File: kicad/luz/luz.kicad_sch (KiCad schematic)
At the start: 58 parts, among them J1 Barrel_Jack, J2 Screw_Terminal_01x04, Q1 AO3400A, Q4 AO3400A, U1 U261-241N-4BS2SS, U2 CYPD3177-24LQXQ_C2959321, U3 SI4909DY-VB, U4 TPS54302, U5 ESP32-WROOM-32D

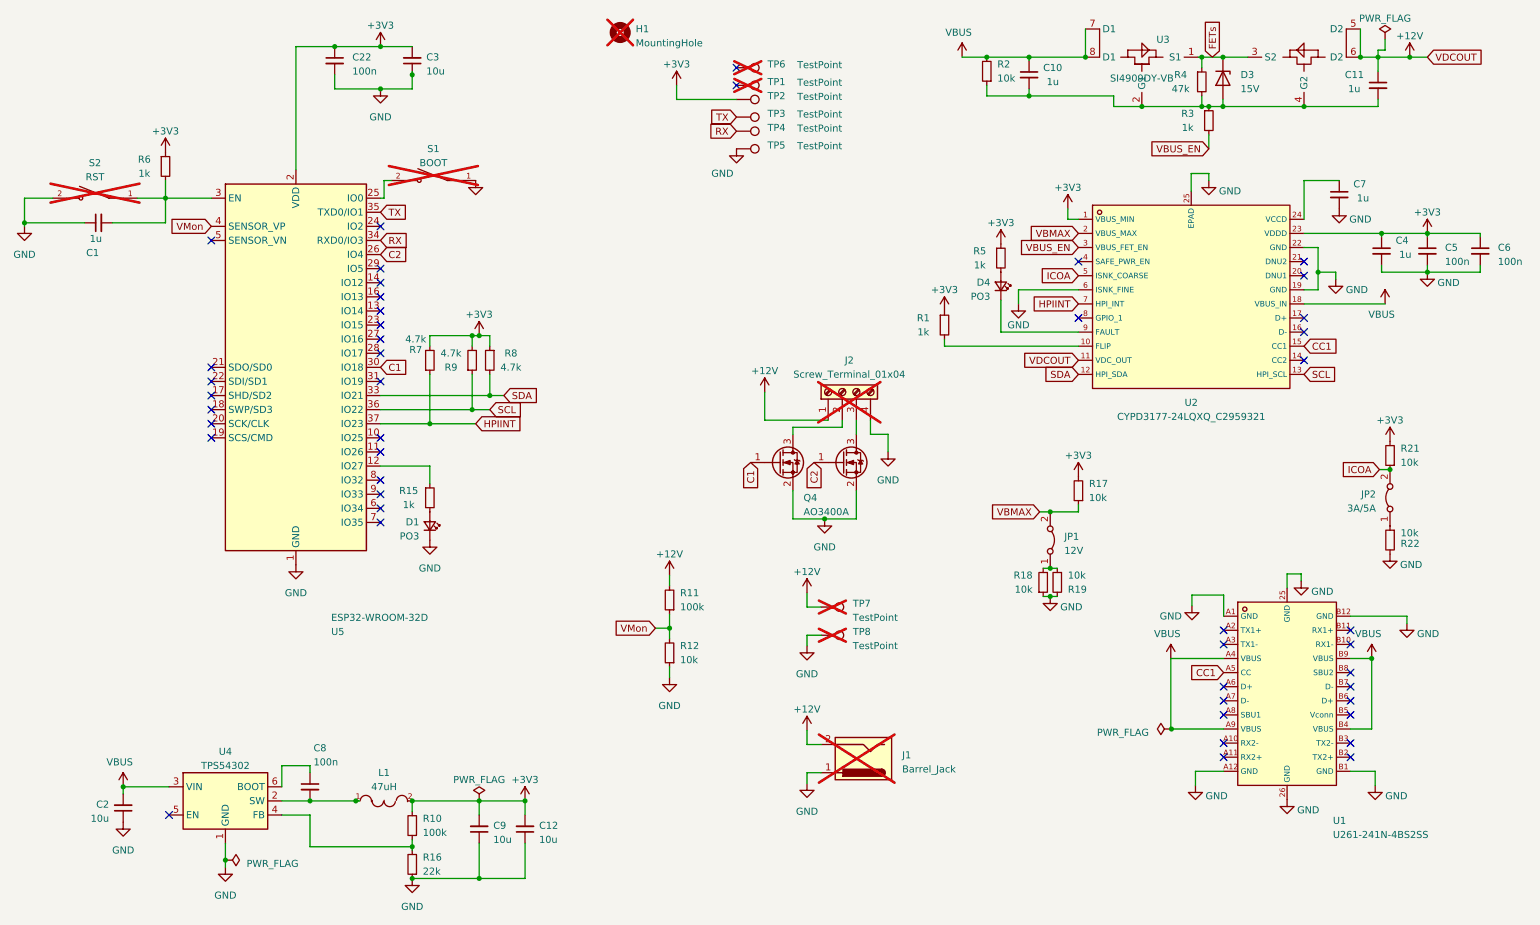
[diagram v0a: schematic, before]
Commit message: Adds 470 resistors to N FET channel drivers' gates & fix VBUSMAX
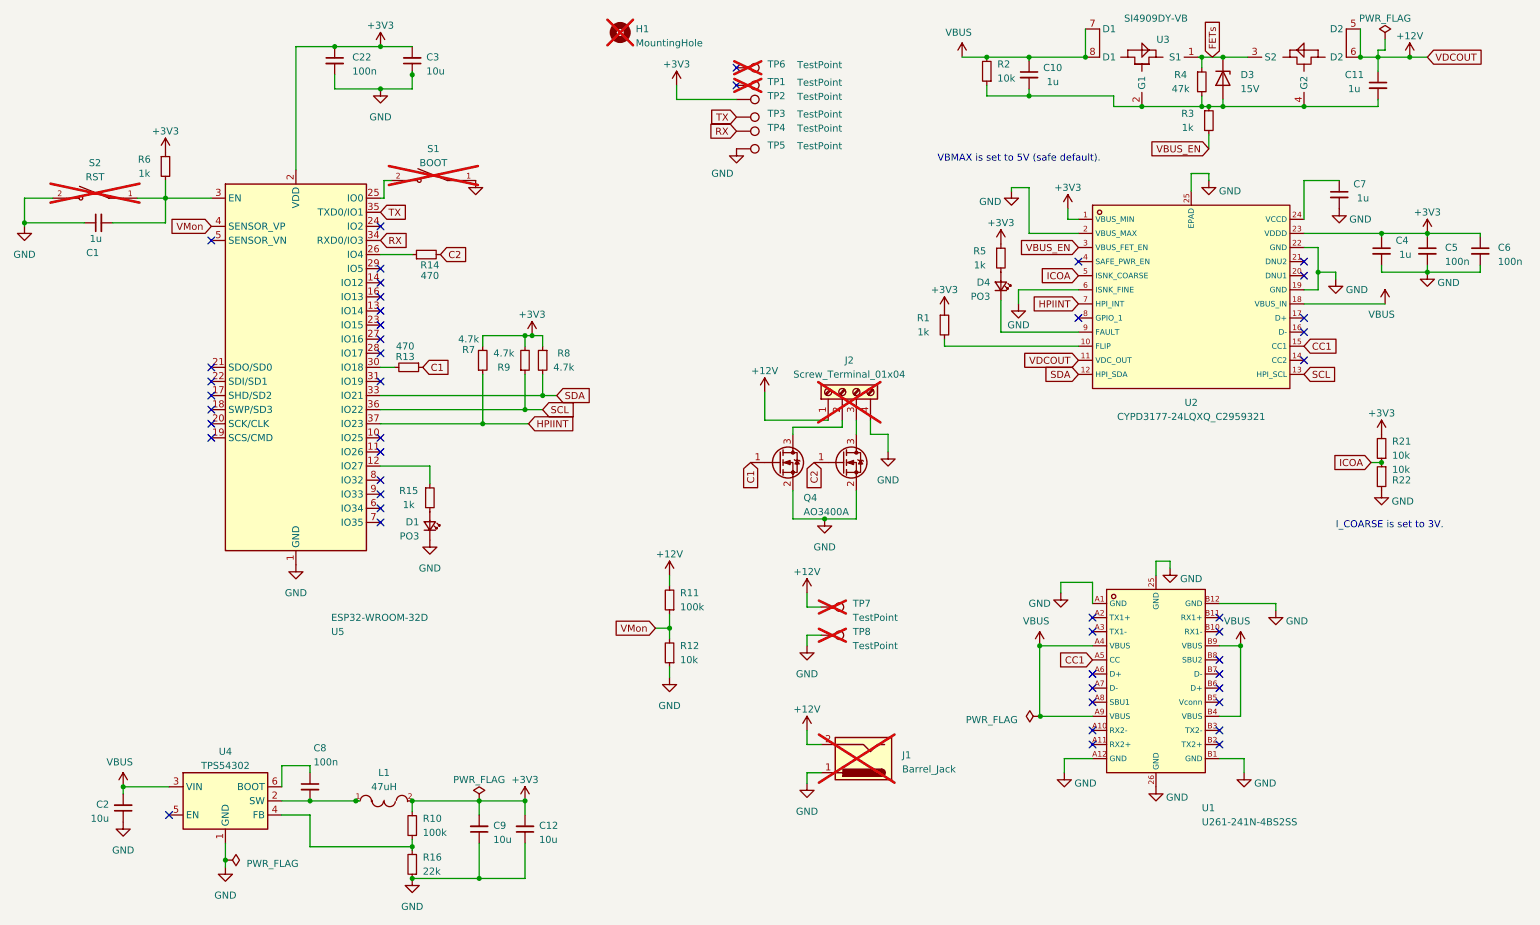
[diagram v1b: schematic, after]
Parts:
- removed JP1: 12V, Jumper:SolderJumper-2_P1.3mm_Bridged_RoundedPad1.0x1.5mm, symbol Jumper:Jumper_2_Bridged
- removed JP2: 3A/5A, Jumper:SolderJumper-2_P1.3mm_Bridged_RoundedPad1.0x1.5mm, symbol Jumper:Jumper_2_Bridged
- removed R17, R18, R19: 10k, Resistor_SMD:R_0402_1005Metric, symbol Device:R_Small
- added R13, R14: 470, Resistor_SMD:R_0402_1005Metric, symbol Device:R_Small
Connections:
- net VBMAX is gone; now on net GND: U2.2 (VBUS_MAX)
- net C1: now also R13.1; no longer U5.30 (IO18)
- net C2: now also R14.2; no longer U5.26 (IO4)
- net ICOA: now also R22.1
- new net: R13.2, U5.30 (IO18)
- new net: R14.1, U5.26 (IO4)
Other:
- note added: "I_COARSE is set to 3V."
- note added: "VBMAX is set to 5V (safe default)."
- moved on the sheet: R21, R22, R7, R8, R9, U1

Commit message: Plotted fab outputs for 0.0.3a
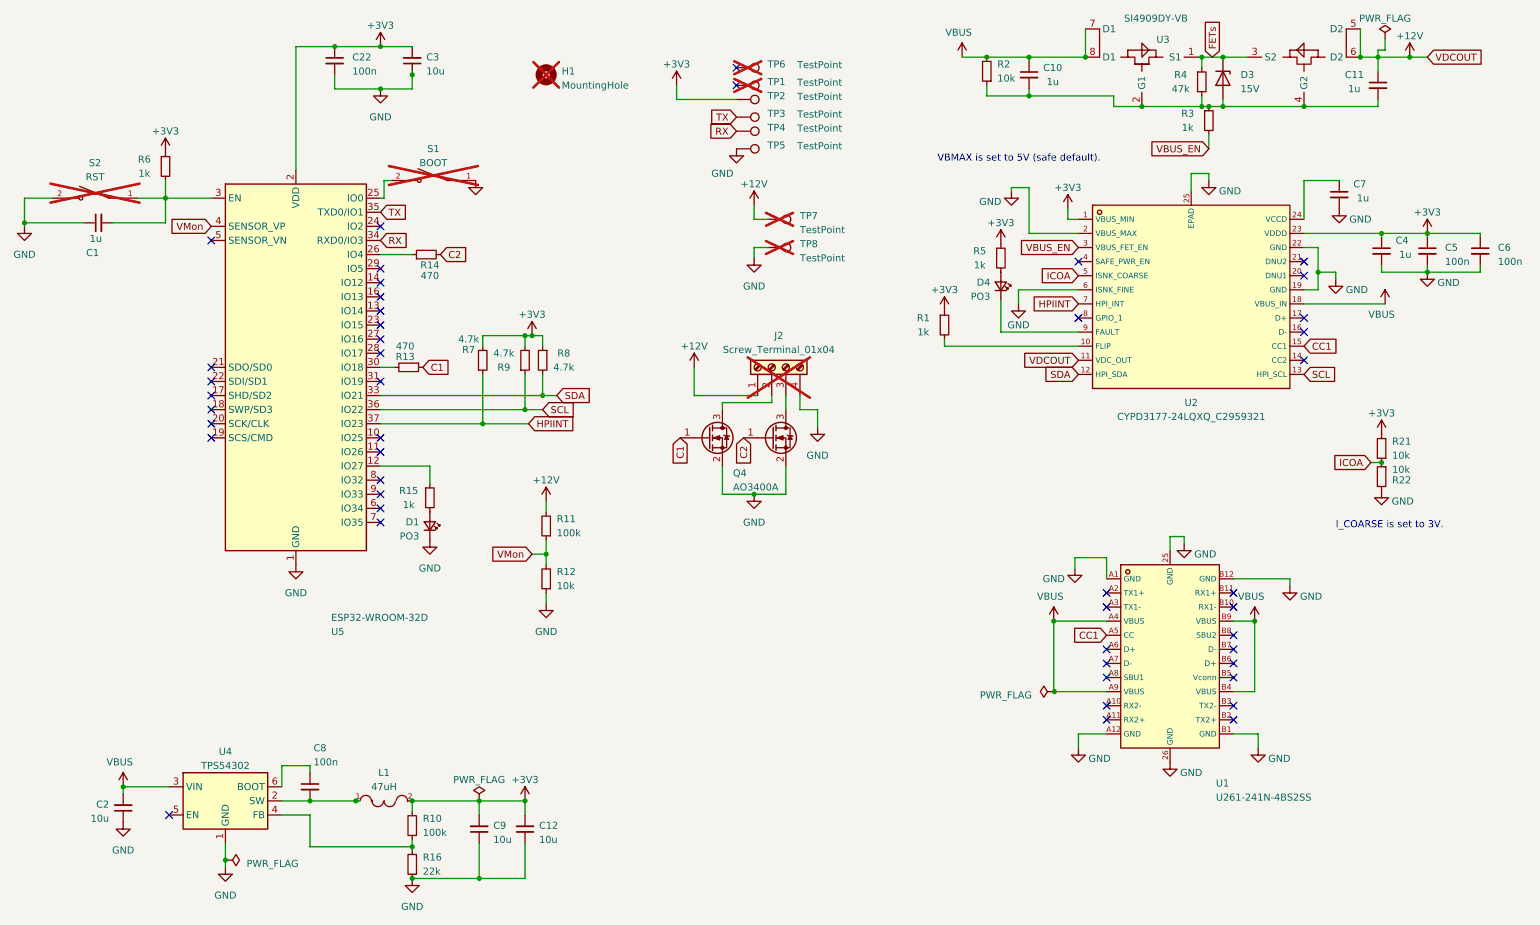
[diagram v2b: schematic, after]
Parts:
- removed J1: Barrel_Jack, Connector_BarrelJack:BarrelJack_CLIFF_FC681465S_SMT_Horizontal, symbol Connector:Barrel_Jack
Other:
- company: (none) -> github.com/rbaron/luz
- title: (none) -> luz
- moved on the sheet: H1, J2, Q4, R11, R12, TP7, TP8, U1
